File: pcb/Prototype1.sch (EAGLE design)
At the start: 30 parts, among them IC1 78L05SMD, Q1 FDS5680, U1 PIC16F1823-X_SL

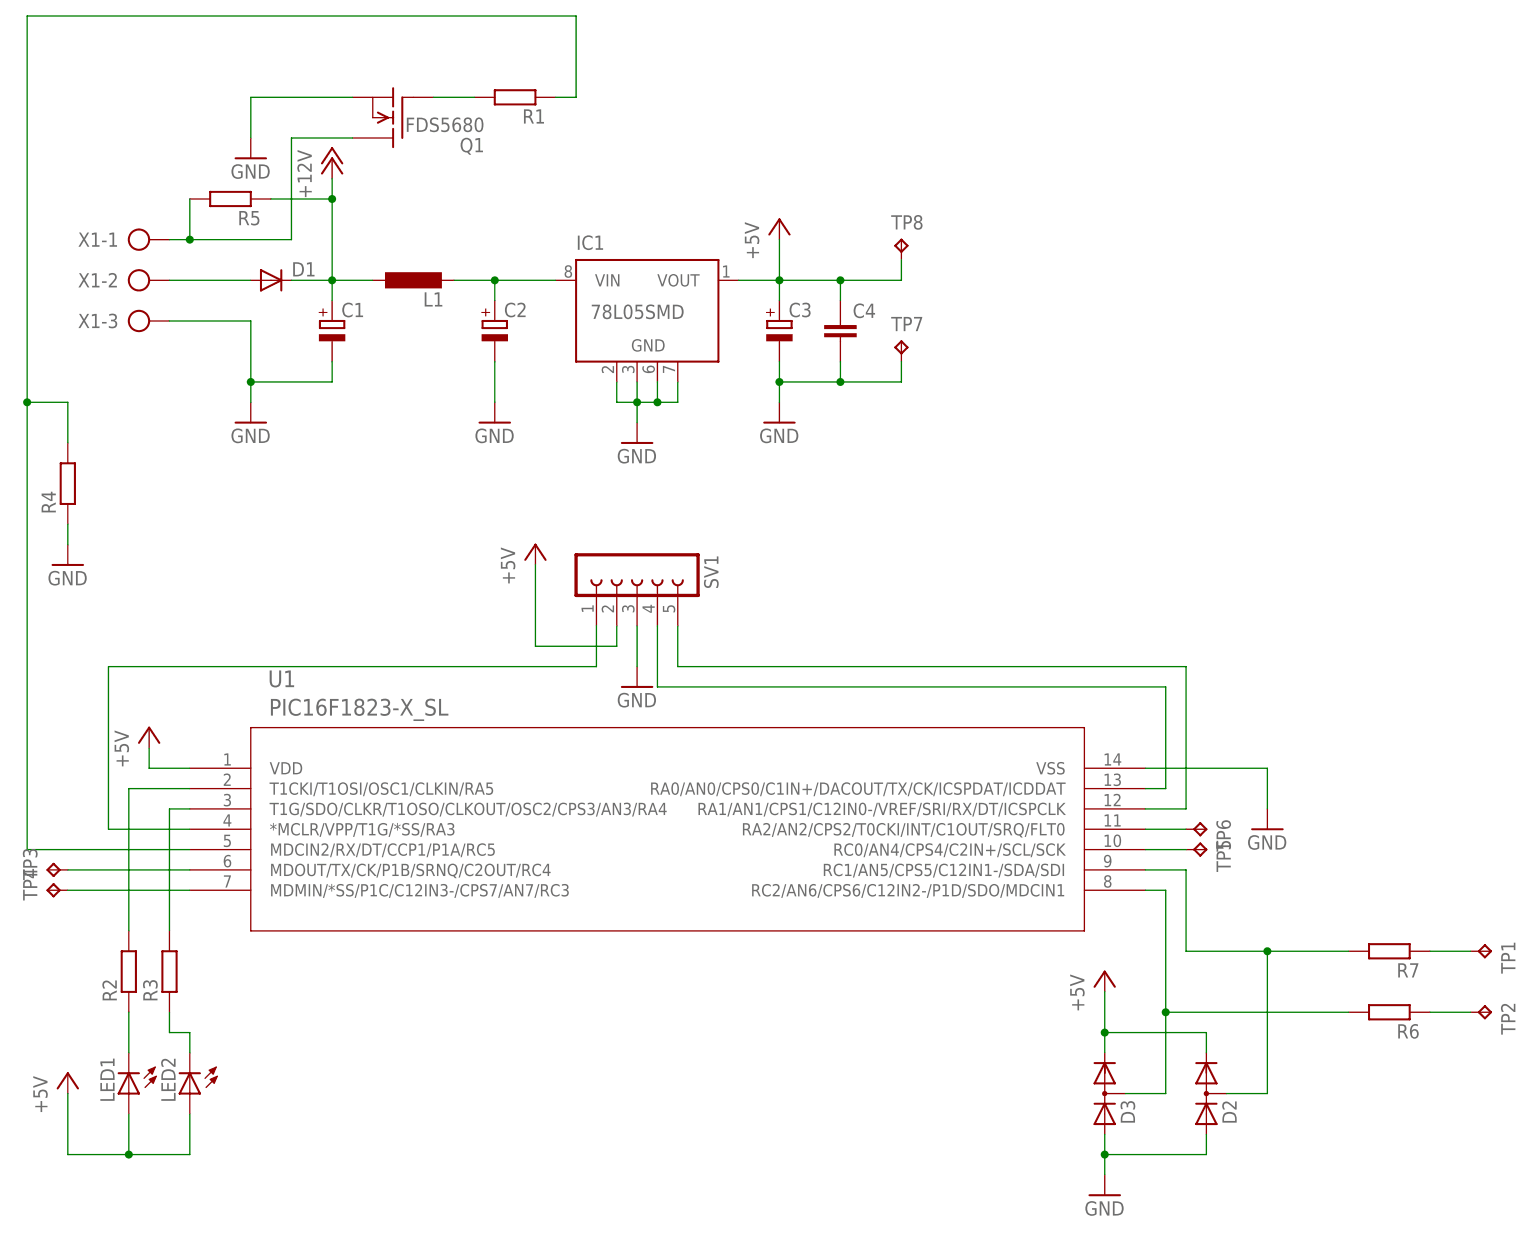
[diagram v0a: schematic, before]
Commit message: Added waveforms, added component values to schematic. Added fail description, and lesson learned to readme.
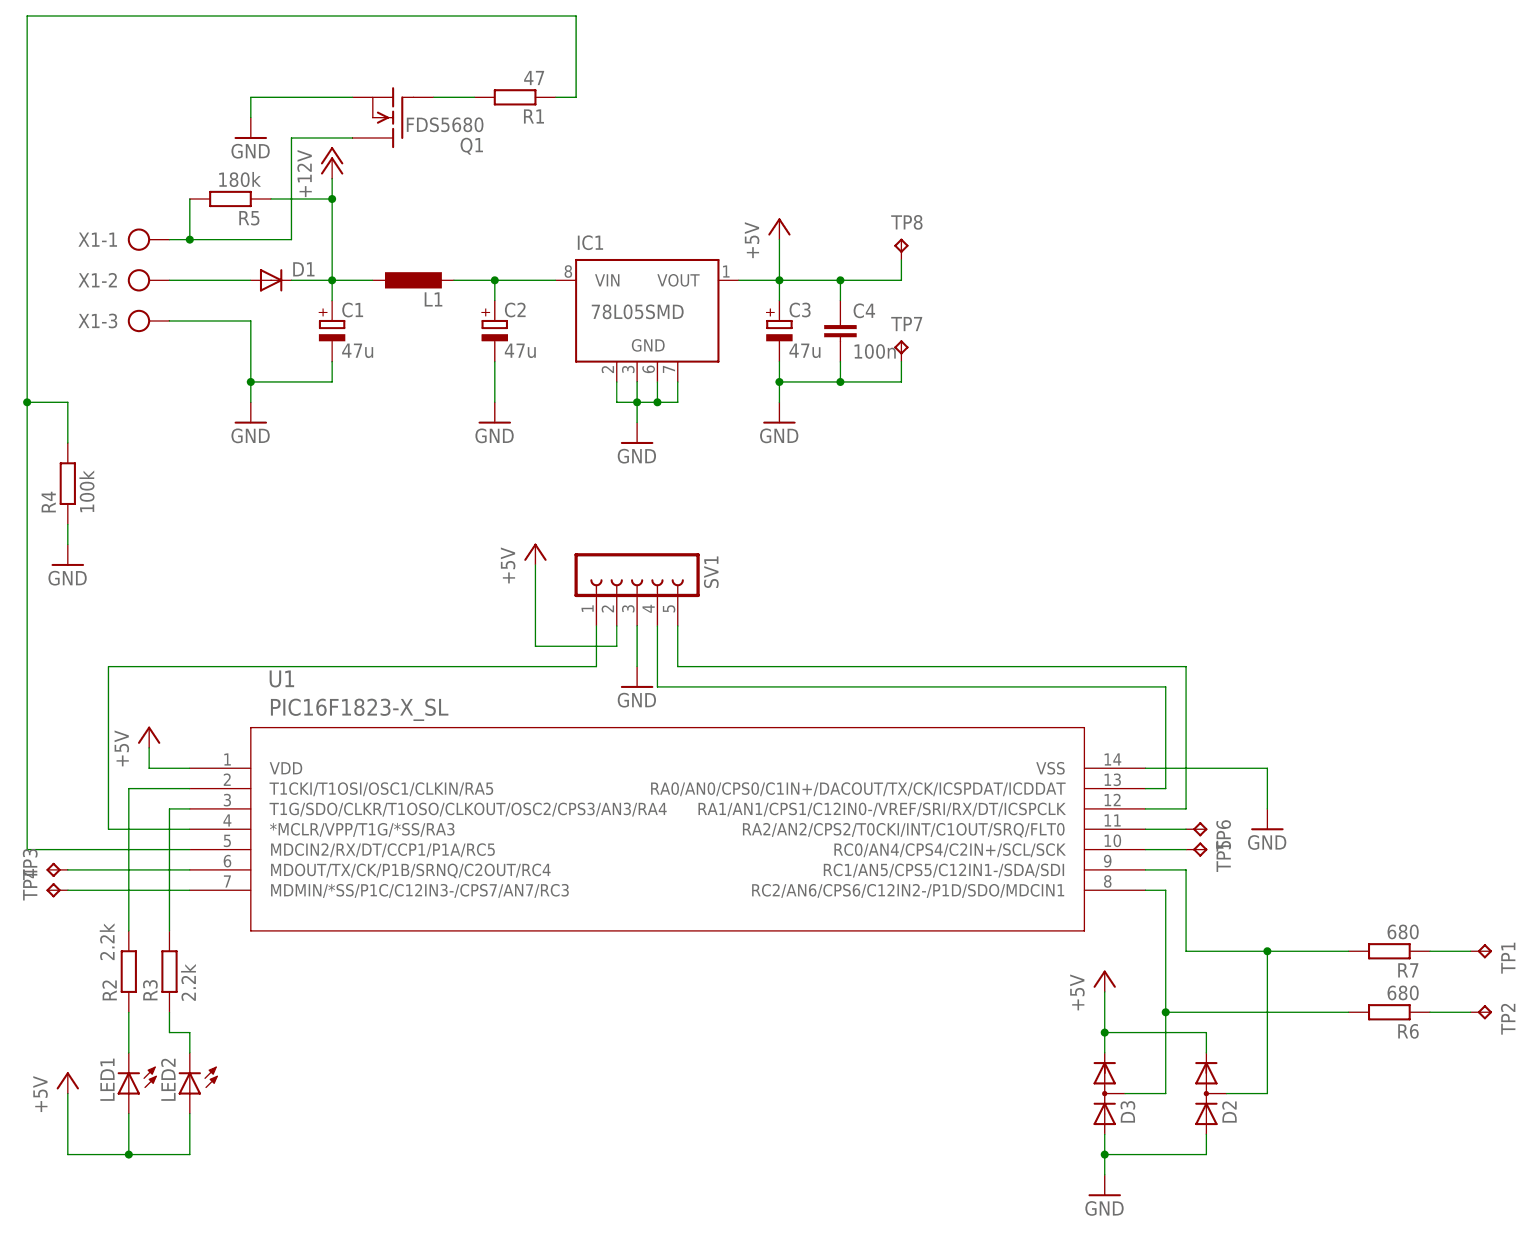
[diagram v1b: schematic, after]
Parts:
- C1, C2, C3: value (none) -> 47u
- C4: value (none) -> 100n
- R1: value (none) -> 47
- R2, R3: value (none) -> 2.2k
- R4: value (none) -> 100k
- R5: value (none) -> 180k
- R6, R7: value (none) -> 680
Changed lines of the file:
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@@
 <grid distance="0.1" unitdist="inch" unit="inch" style="lines" multiple="1" display="no" altdistance="0.01" altunitdist="inch" altunit="inch"/>
 <layers>
-<layer number="1" name="Top" color="4" fill="1" visible="yes" active="no"/>
-<layer number="16" name="Bottom" color="1" fill="1" visible="yes" active="no"/>
-<layer number="17" name="Pads" color="2" fill="1" visible="yes" active="no"/>
-<layer number="18" name="Vias" color="2" fill="1" visible="yes" active="no"/>
-<layer number="19" name="Unrouted" color="6" fill="1" visible="yes" active="no"/>
-<layer number="20" name="Dimension" color="15" fill="1" visible="yes" active="no"/>
-<layer number="21" name="tPlace" color="7" fill="1" visible="yes" active="no"/>
-<layer number="22" name="bPlace" color="7" fill="1" visible="yes" active="no"/>
-<layer number="23" name="tOrigins" color="15" fill="1" visible="yes" active="no"/>
-<layer number="24" name="bOrigins" color="15" fill="1" visible="yes" active="no"/>
-<layer number="25" name="tNames" color="7" fill="1" visible="yes" active="no"/>
-<layer number="26" name="bNames" color="7" fill="1" visible="yes" active="no"/>
-<layer number="27" name="tValues" color="7" fill="1" visible="yes" active="no"/>
-<layer number="28" name="bValues" color="7" fill="1" visible="yes" active="no"/>
+<layer number="1" name="Top" color="4" fill="1" visible="no" active="no"/>
+<layer number="16" name="Bottom" color="1" fill="1" visible="no" active="no"/>
+<layer number="17" name="Pads" color="2" fill="1" visible="no" active="no"/>
+<layer number="18" name="Vias" color="2" fill="1" visible="no" active="no"/>
+<layer number="19" name="Unrouted" color="6" fill="1" visible="no" active="no"/>
+<layer number="20" name="Dimension" color="15" fill="1" visible="no" active="no"/>
+<layer number="21" name="tPlace" color="7" fill="1" visible="no" active="no"/>
+<layer number="22" name="bPlace" color="7" fill="1" visible="no" active="no"/>
+<layer number="23" name="tOrigins" color="15" fill="1" visible="no" active="no"/>
+<layer number="24" name="bOrigins" color="15" fill="1" visible="no" active="no"/>
+<layer number="25" name="tNames" color="7" fill="1" visible="no" active="no"/>
+<layer number="26" name="bNames" color="7" fill="1" visible="no" active="no"/>
+<layer number="27" name="tValues" color="7" fill="1" visible="no" active="no"/>
+<layer number="28" name="bValues" color="7" fill="1" visible="no" active="no"/>
 <layer number="29" name="tStop" color="7" fill="3" visible="no" active="no"/>
 <layer number="30" name="bStop" color="7" fill="6" visible="no" active="no"/>
@@
 <layer number="35" name="tGlue" color="7" fill="4" visible="no" active="no"/>
 <layer number="36" name="bGlue" color="7" fill="5" visible="no" active="no"/>
-<layer number="37" name="tTest" color="7" fill="1" visible="yes" active="no"/>
-<layer number="38" name="bTest" color="7" fill="1" visible="yes" active="no"/>
+<layer number="37" name="tTest" color="7" fill="1" visible="no" active="no"/>
+<layer number="38" name="bTest" color="7" fill="1" visible="no" active="no"/>
 <layer number="39" name="tKeepout" color="4" fill="11" visible="no" active="no"/>
 <layer number="40" name="bKeepout" color="1" fill="11" visible="no" active="no"/>
@@
 <layer number="44" name="Drills" color="7" fill="1" visible="no" active="no"/>
 <layer number="45" name="Holes" color="7" fill="1" visible="no" active="no"/>
-<layer number="46" name="Milling" color="3" fill="1" visible="yes" active="no"/>
-<layer number="47" name="Measures" color="7" fill="1" visible="yes" active="no"/>
-<layer number="48" name="Document" color="7" fill="1" visible="yes" active="no"/>
-<layer number="49" name="Reference" color="7" fill="1" visible="yes" active="no"/>
-<layer number="51" name="tDocu" color="7" fill="1" visible="yes" active="no"/>
-<layer number="52" name="bDocu" color="7" fill="1" visible="yes" active="no"/>
+<layer number="46" name="Milling" color="3" fill="1" visible="no" active="no"/>
+<layer number="47" name="Measures" color="7" fill="1" visible="no" active="no"/>
+<layer number="48" name="Document" color="7" fill="1" visible="no" active="no"/>
+<layer number="49" name="Reference" color="7" fill="1" visible="no" active="no"/>
+<layer number="51" name="tDocu" color="7" fill="1" visible="no" active="no"/>
+<layer number="52" name="bDocu" color="7" fill="1" visible="no" active="no"/>
 <layer number="90" name="Modules" color="5" fill="1" visible="yes" active="yes"/>
 <layer number="91" name="Nets" color="2" fill="1" visible="yes" active="yes"/>
@@
 <part name="U1" library="microchip_pic16" deviceset="PIC16F1823-X_SL" device=""/>
 <part name="Q1" library="transistor-fet" deviceset="FDS5680" device=""/>
-<part name="C1" library="rcl" deviceset="CPOL-EU" device="153CLV-0605"/>
-<part name="C2" library="rcl" deviceset="CPOL-EU" device="153CLV-0605"/>
-<part name="C3" library="rcl" deviceset="CPOL-EU" device="153CLV-0605"/>
+<part name="C1" library="rcl" deviceset="CPOL-EU" device="153CLV-0605" value="47u"/>
+<part name="C2" library="rcl" deviceset="CPOL-EU" device="153CLV-0605" value="47u"/>
+<part name="C3" library="rcl" deviceset="CPOL-EU" device="153CLV-0605" value="47u"/>
 <part name="L1" library="rcl" deviceset="L-EU" device="L3230M"/>
 <part name="D1" library="diode" deviceset="DIODE-" device="MELF-MLL41"/>
 <part name="SV1" library="con-lsta" deviceset="FE05-1" device=""/>
-<part name="R1" library="rcl" deviceset="R-EU_" device="M1206"/>
-<part name="R2" library="rcl" deviceset="R-EU_" device="M1206"/>
-<part name="R3" library="rcl" deviceset="R-EU_" device="M1206"/>
+<part name="R1" library="rcl" deviceset="R-EU_" device="M1206" value="47"/>
+<part name="R2" library="rcl" deviceset="R-EU_" device="M1206" value="2.2k"/>
+<part name="R3" library="rcl" deviceset="R-EU_" device="M1206" value="2.2k"/>
 <part name="IC1" library="linear" deviceset="78L*SMD" device="" technology="05"/>
 <part name="X1" library="con-ptr500" deviceset="AK500/3" device=""/>
@@
 <part name="P+4" library="supply1" deviceset="+5V" device=""/>
 <part name="GND7" library="supply1" deviceset="GND" device=""/>
-<part name="R4" library="rcl" deviceset="R-EU_" device="M1206"/>
+<part name="R4" library="rcl" deviceset="R-EU_" device="M1206" value="100k"/>
 <part name="GND8" library="supply1" deviceset="GND" device=""/>
 <part name="D2" library="diode" deviceset="DIODE_2CACA-" device="SOT23"/>
@@
 <part name="TP1" library="testpad" deviceset="TP" device="PAD1-13Y"/>
 <part name="TP2" library="testpad" deviceset="TP" device="PAD1-13Y"/>
-<part name="R5" library="rcl" deviceset="R-EU_" device="M1206"/>
-<part name="C4" library="rcl" deviceset="C-EU" device="C0805"/>
-<part name="R6" library="rcl" deviceset="R-EU_" device="M1206"/>
-<part name="R7" library="rcl" deviceset="R-EU_" device="M1206"/>
+<part name="R5" library="rcl" deviceset="R-EU_" device="M1206" value="180k"/>
+<part name="C4" library="rcl" deviceset="C-EU" device="C0805" value="100n"/>
+<part name="R6" library="rcl" deviceset="R-EU_" device="M1206" value="680"/>
+<part name="R7" library="rcl" deviceset="R-EU_" device="M1206" value="680"/>
 <part name="LED1" library="led" deviceset="LED" device="SML1206"/>
 <part name="LED2" library="led" deviceset="LED" device="SML1206"/>
@@
 <instance part="SV1" gate="G$1" x="27.94" y="20.32" rot="R270"/>
 <instance part="R1" gate="G$1" x="12.7" y="78.74" rot="R180"/>
-<instance part="R2" gate="G$1" x="-35.56" y="-30.48" rot="R90"/>
+<instance part="R2" gate="G$1" x="-35.56" y="-30.48" smashed="yes" rot="R90">
+<attribute name="NAME" x="-37.0586" y="-34.29" size="1.778" layer="95" rot="R90"/>
+<attribute name="VALUE" x="-37.338" y="-29.21" size="1.778" layer="96" rot="R90"/>
+</instance>
 <instance part="R3" gate="G$1" x="-30.48" y="-30.48" rot="R90"/>
 <instance part="IC1" gate="G$1" x="27.94" y="55.88"/>
@@
 <instance part="X1" gate="-3" x="-35.56" y="50.8"/>
 <instance part="GND1" gate="1" x="-20.32" y="38.1"/>
-<instance part="GND2" gate="1" x="-20.32" y="71.12"/>
+<instance part="GND2" gate="1" x="-20.32" y="73.66"/>
 <instance part="GND3" gate="1" x="27.94" y="35.56"/>
 <instance part="GND4" gate="1" x="27.94" y="5.08"/>
@@
 <pinref part="GND2" gate="1" pin="GND"/>
 <pinref part="Q1" gate="G$1" pin="S"/>
-<wire x1="-20.32" y1="73.66" x2="-20.32" y2="78.74" width="0.1524" layer="91"/>
+<wire x1="-20.32" y1="76.2" x2="-20.32" y2="78.74" width="0.1524" layer="91"/>
 <wire x1="-20.32" y1="78.74" x2="-7.62" y2="78.74" width="0.1524" layer="91"/>
 </segment>
